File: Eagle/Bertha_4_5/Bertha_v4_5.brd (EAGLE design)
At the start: 100 x 83.6 mm, 132 parts, among them CON1 JACK_DC_BARREL, CON2 JACK_DC_BARREL, IC1 MCP1703DB, IC4 DRV8811, J1 RJ12RIGHTANGLE-I2C, J2 RJ12RIGHTANGLE-I2C, Q5 BSP75, Q6 BSP75, U1 HX711, U100 RN2483, X1 1503_09, X2 8MHz, X3 FH12-08S-1SH, X4 MINI-USB

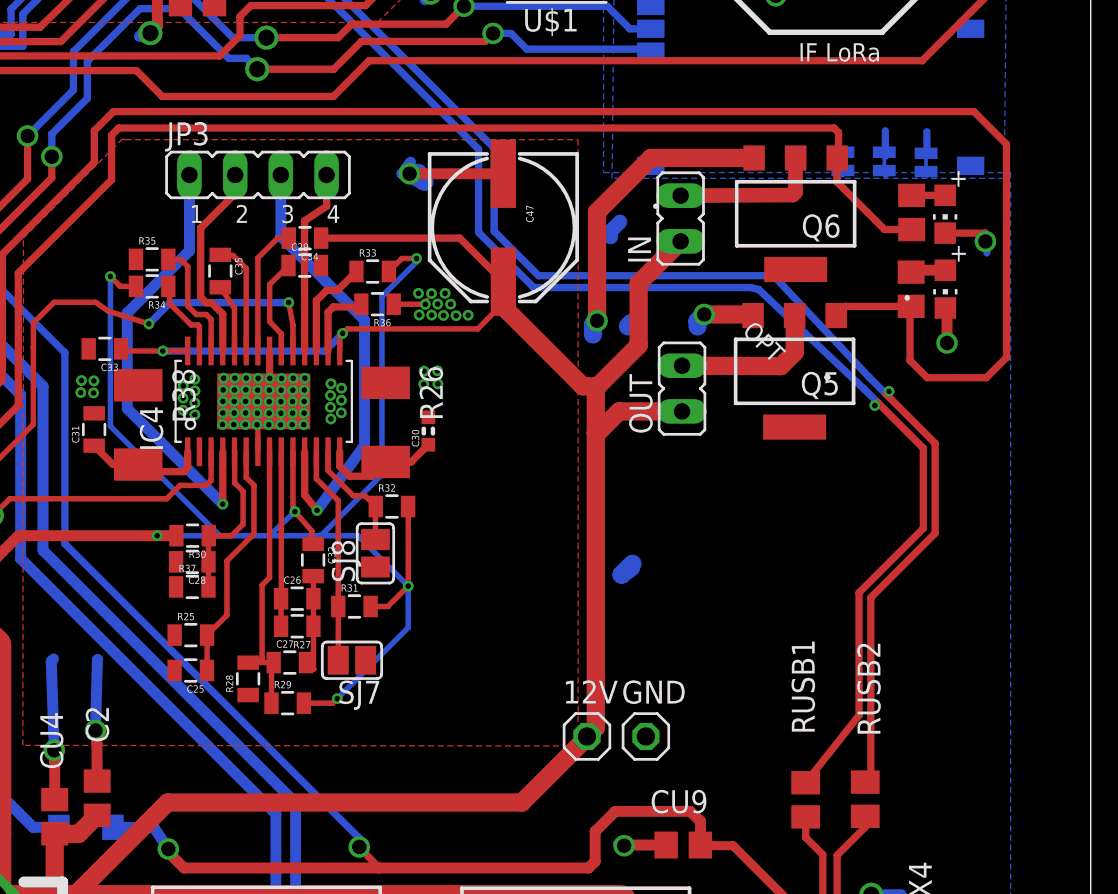
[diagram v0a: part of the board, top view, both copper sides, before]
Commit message: Moved pumps downward to prepare for LoRa antenna migration
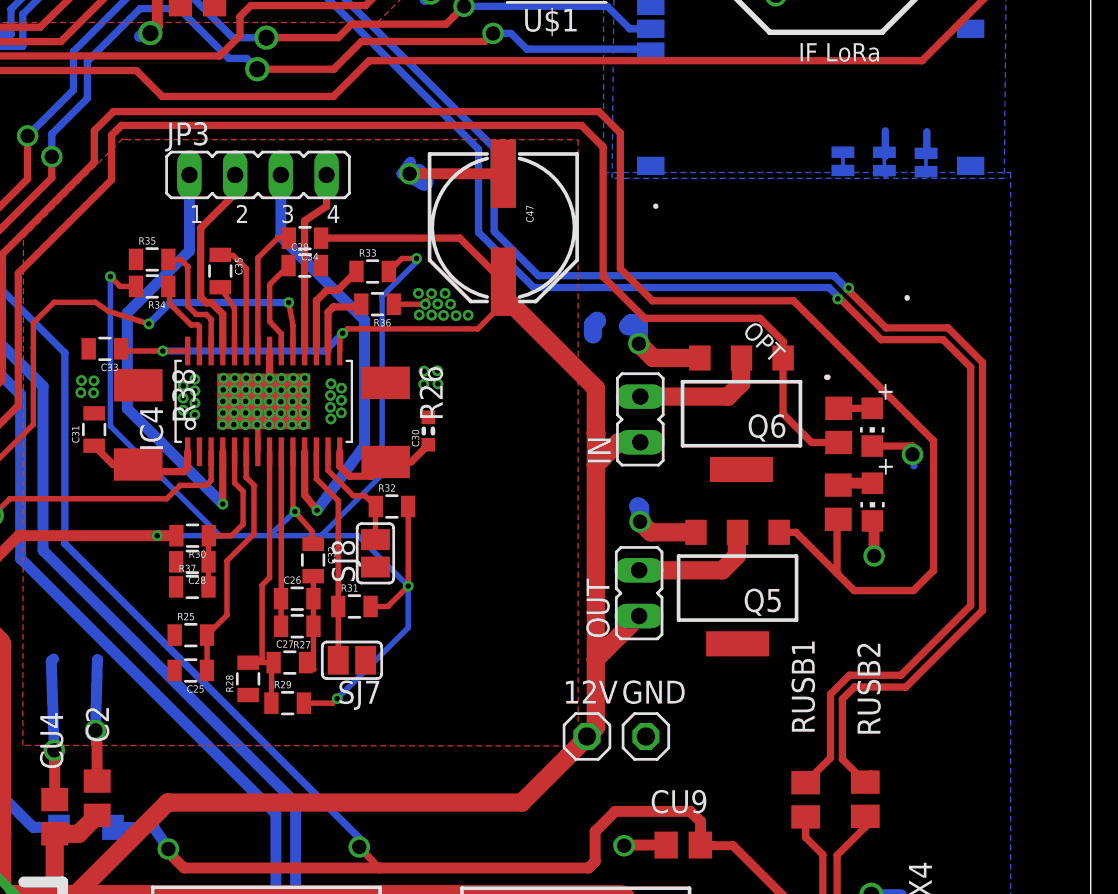
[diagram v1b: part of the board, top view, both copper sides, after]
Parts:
- moved RK12 12.5 mm to (81.0, 35.4)
- moved LDIN 12.5 mm to (82.9, 35.3)
- moved LDOUT 12.5 mm to (82.9, 31.1)
- moved RK13 12.5 mm to (81.0, 31.1)
- moved Q5 12.5 mm to (75.4, 26.3)
- moved OUT 11.6 mm to (69.9, 26.1)
- moved Q6 11.5 mm to (75.6, 36.0)
- moved IN 11.4 mm to (70.0, 35.7)
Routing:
- net GND: track 172.6 -> 159.4 mm
- net USB_P: track 111.2 -> 120.5 mm
- net +12V: track 244.9 -> 235.8 mm
- net USB_N: track 109.6 -> 117.7 mm
- net N$8: track 78.5 -> 84.3 mm
- net N$11: track 102.2 -> 104.5 mm
- net N$13: track 8.64 -> 7.09 mm
- net N$17: track 8.36 -> 7.33 mm
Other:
- board text added: "PUMPS"

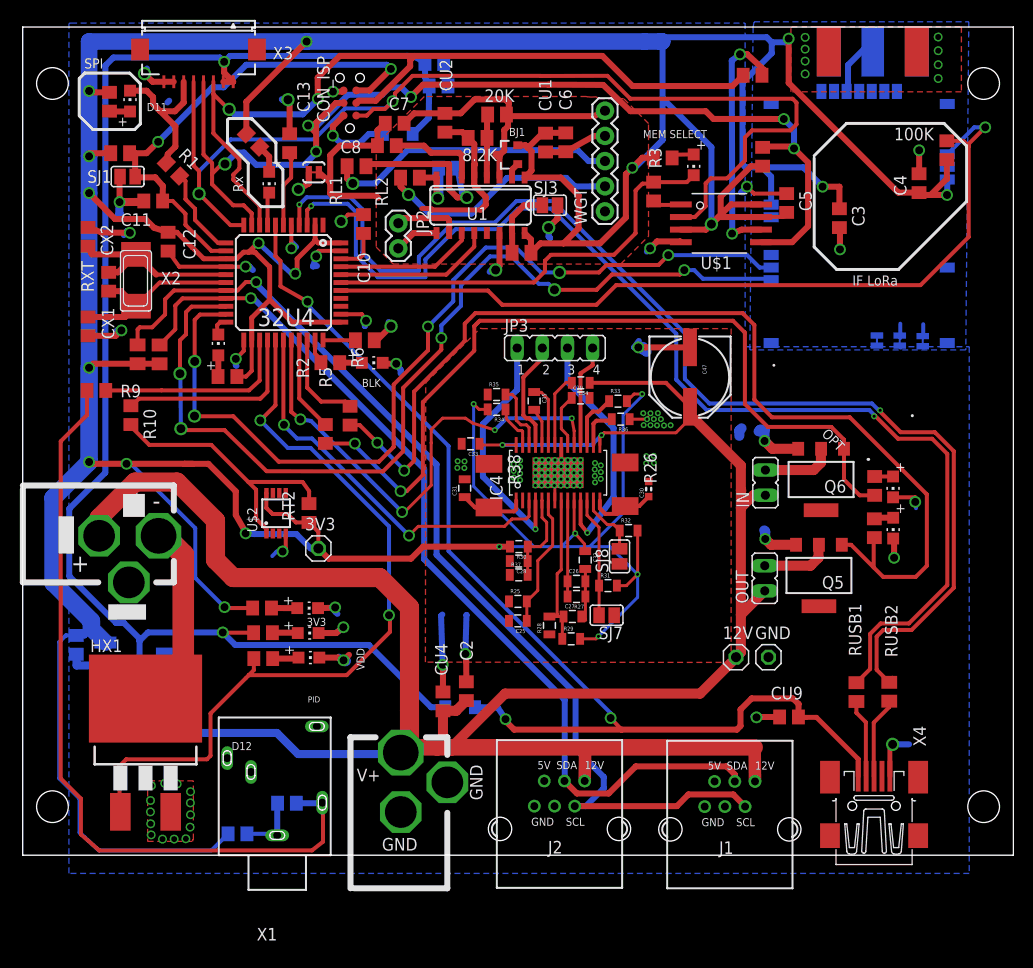
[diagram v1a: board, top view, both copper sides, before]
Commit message: LoRa Antenna moved inward, rerouted more simply the SST Flash memory closes #85 closes #86 closes #87, need to regen Gerbers
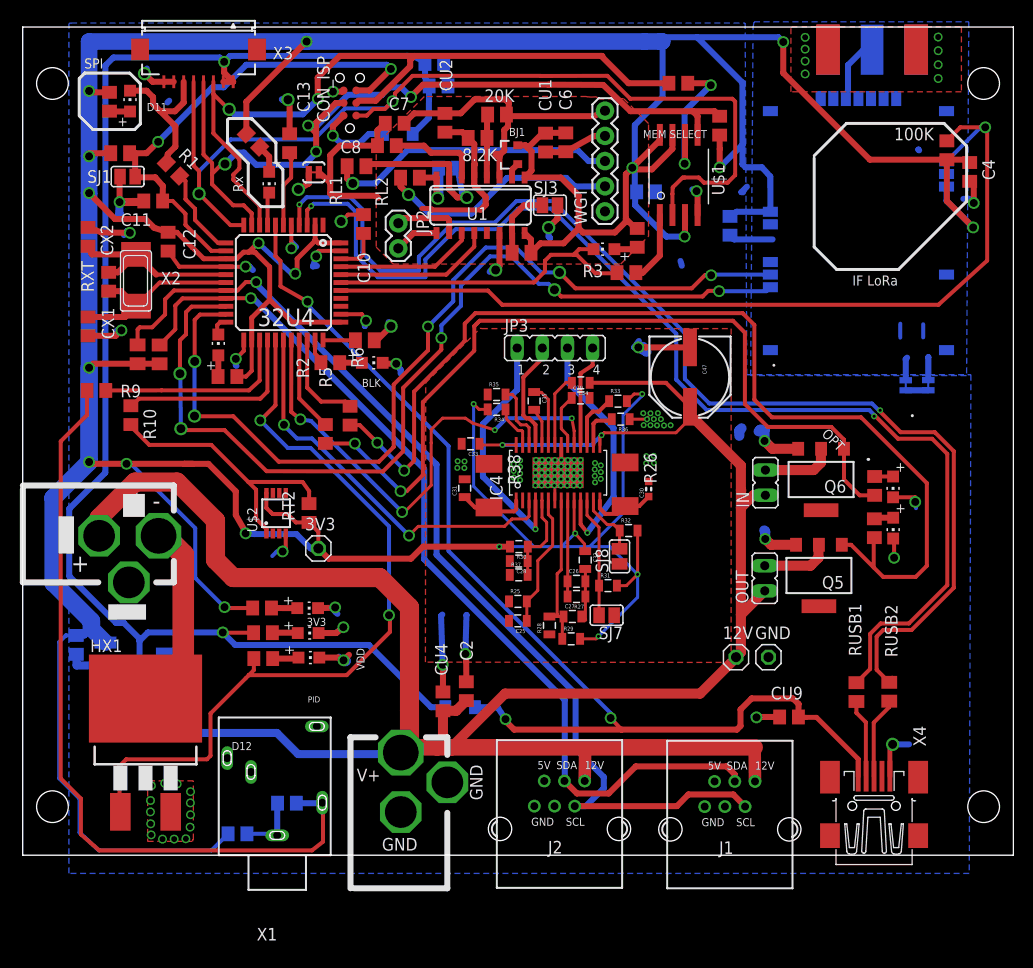
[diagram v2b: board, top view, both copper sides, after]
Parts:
- removed SJ6: (no value), SparkFun-Passives:PAD-JUMPER-2-NC_BY_TRACE_YES_SILK
- U$1: value SST25VF064C -> SST26VF064B
- moved C5 14.2 mm to (57.9, 65.1), flipped to the bottom, turned to 0 degrees
- moved LDMEM 12.4 mm to (53.7, 59.3), turned to 90 degrees
- moved C3 11.1 mm to (66.4, 61.6), flipped to the bottom
- moved R3 8.63 mm to (55.9, 56.9), turned to 180 degrees
- moved RK19 8.47 mm to (57.0, 60.4), turned to 270 degrees
- moved RK3 7.54 mm to (61.2, 76.0)
- moved SJ5 5.37 mm to (84.1, 45.5)
- moved RK4 5.36 mm to (65.4, 71.7)
- moved SJ4 5.34 mm to (86.4, 45.5)
- moved C4 5.24 mm to (90.6, 67.1), turned to 270 degrees
- moved U$1 4.91 mm to (61.2, 65.7), turned to 0 degrees
- moved U100 0.72 mm to (88.3, 47.8)
- moved 868MHZ 0.19 mm to (80.7, 82.0)
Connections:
- net ANGND: no longer SJ6.2
- net GND: no longer SJ6.1
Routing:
- net MOSI: track 109.8 -> 85.2 mm, vias 6 -> 4
- net N$23: track 25.2 -> 14.4 mm
- net A3: track 43.3 -> 32.7 mm
- net 3.3V: track 574.8 -> 565.1 mm
- net MISO: track 110.1 -> 100.9 mm
- net SCK: track 84.9 -> 76.9 mm
- net ANGND: track 7.76 -> 15.6 mm, vias 10 -> 9
- net A2: track 86.0 -> 90.9 mm
- net MEM_SEL: track 2.93 -> 7.23 mm
- net GND: track 159.4 -> 156.6 mm, vias 119 -> 118
- net N$11: track 104.5 -> 105.2 mm
- net RX: track 95.7 -> 95.1 mm
- net ANT868: track 5.91 -> 6.50 mm

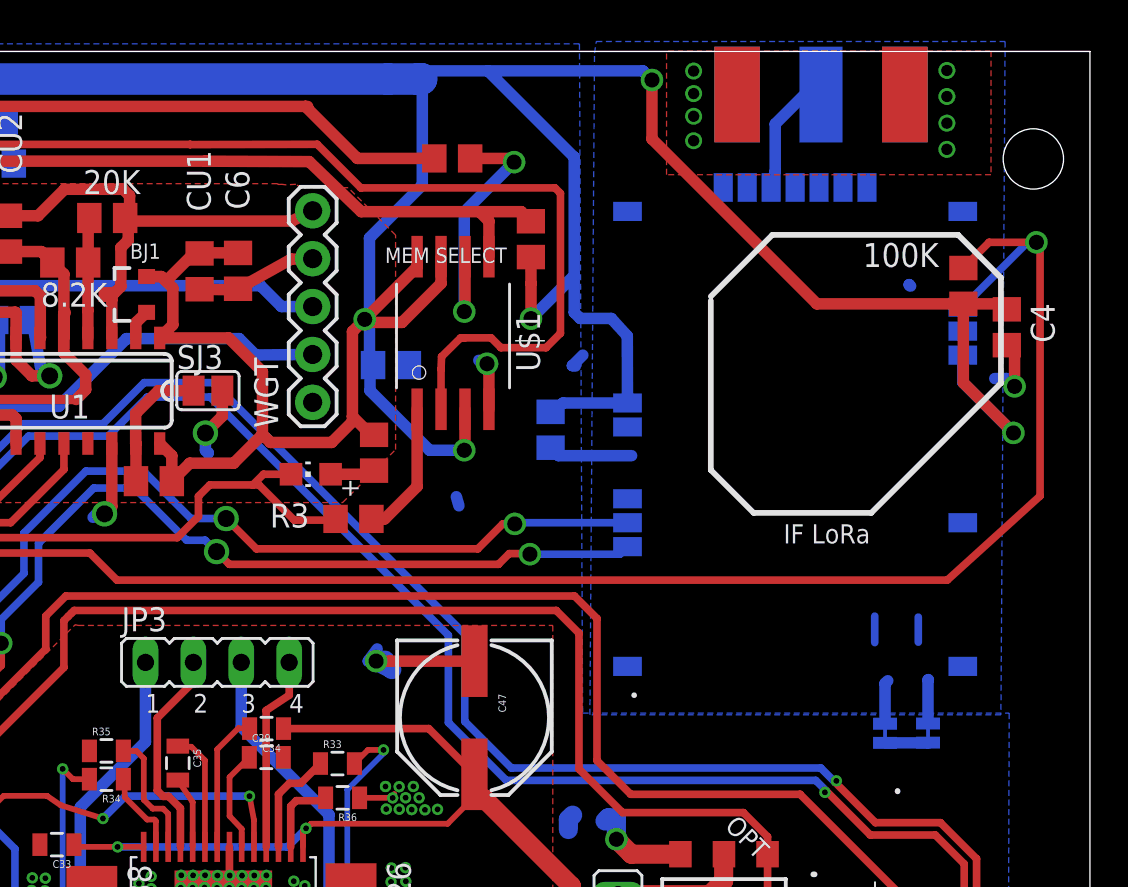
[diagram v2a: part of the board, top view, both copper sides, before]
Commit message: Modified LoRa footprint for ease of soldering Still need to regen Gerbers
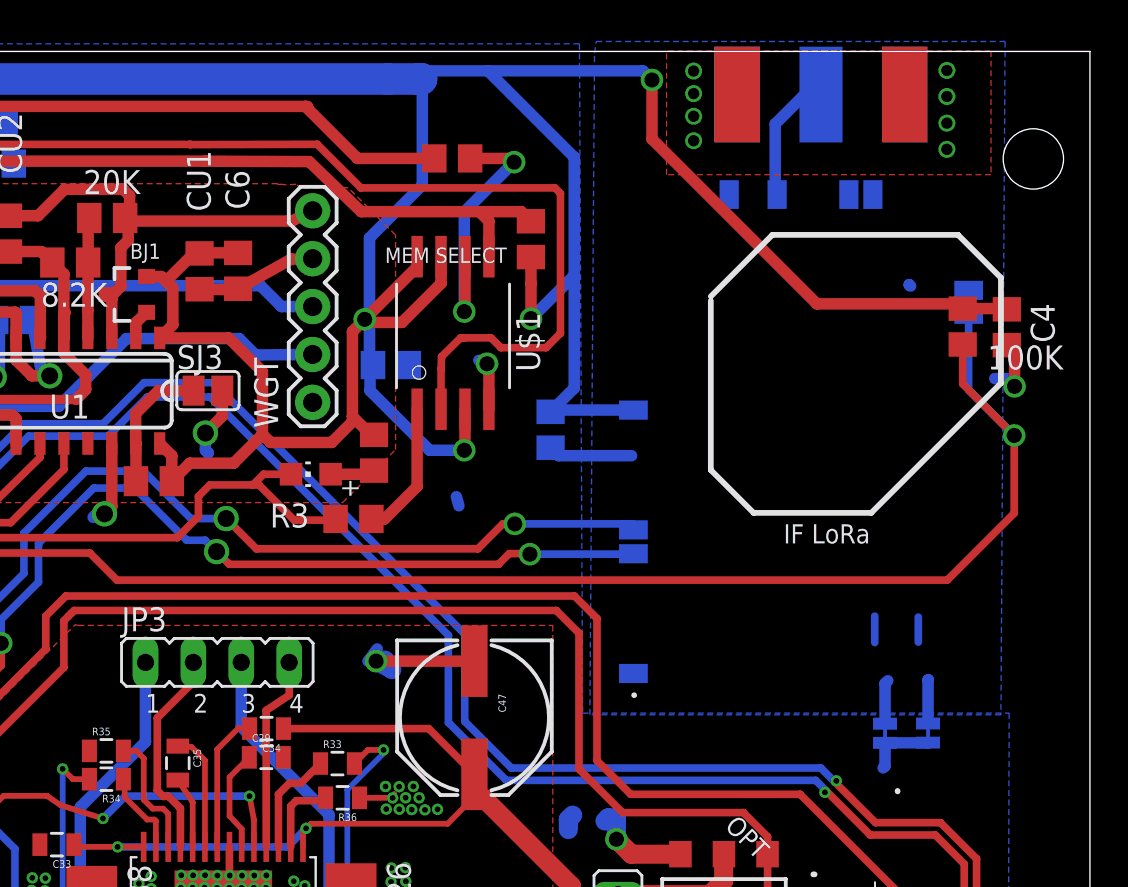
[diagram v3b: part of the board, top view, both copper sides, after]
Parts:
- removed U100: RN2483, Octanis1:RN2483
- added U$3: RN2483_SIMPLE, Octanis1_bioreactorPort:RN2483_SIMPLE
- moved 100K 2.16 mm to (88.3, 67.1), turned to 270 degrees
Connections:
- net 3.3V: now also U$3.P$12; no longer U100.P$12, U100.P$34
- net A2: now also U$3.P$32; no longer U100.P$32
- net ANGND: now also U$3.P$1, U$3.P$21, U$3.P$26, U$3.P$27, U$3.P$33; no longer U100.P$1, U100.P$11, U100.P$20, U100.P$21, U100.P$22, U100.P$24, U100.P$26, U100.P$27, U100.P$28, U100.P$33, U100.P$41, U100.P$47, U100.P$8
- net ANT868: now also U$3.P$23; no longer U100.P$23
- net RX: now also U$3.P$6; no longer U100.P$6
- net TX: now also U$3.P$7; no longer U100.P$7
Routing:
- net 3.3V: track 565.1 -> 551.4 mm, vias 22 -> 21
- net A2: track 90.9 -> 83.5 mm
- net TX: track 90.7 -> 91.4 mm

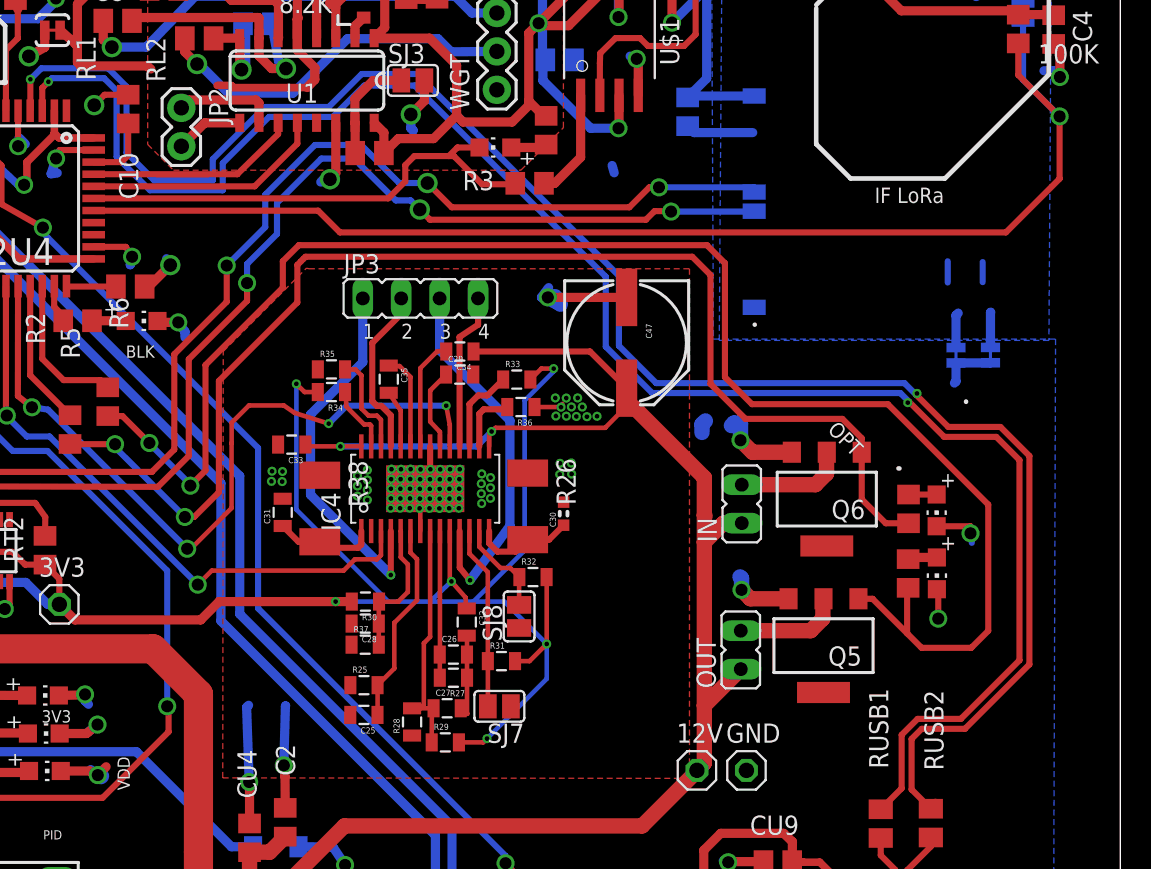
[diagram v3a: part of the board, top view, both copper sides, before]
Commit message: Added LEDs for DRV8811 Stepper Driver closes #83
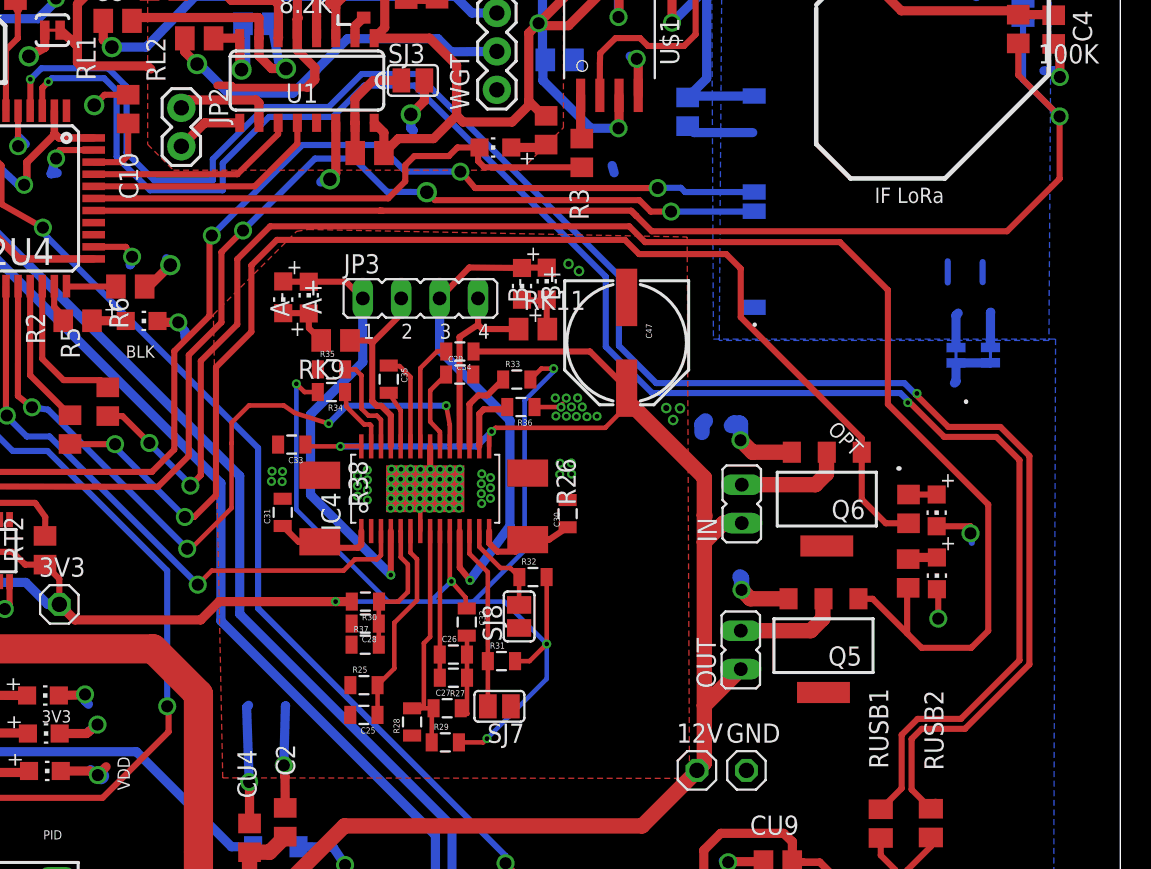
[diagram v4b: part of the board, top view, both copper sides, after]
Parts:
- added A+: A+, adafruit:CHIP-LED0805
- added A-: A-, adafruit:CHIP-LED0805
- added B+: B+, adafruit:CHIP-LED0805
- added B-: B-, adafruit:CHIP-LED0805
- added RK11, RK9: 10k, rcl:R0805
- C30: device freetronics-master-v1:0603 -> freetronics-master-v1:0805
- moved R3 3.99 mm to (59.4, 58.9), turned to 270 degrees
- moved C30 0.27 mm to (58.5, 35.1)
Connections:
- removed net N$10: IC4.25, JP3.2
- removed net N$4: IC4.18, JP3.4
- removed net N$55: IC4.4, JP3.1
- removed net N$56: IC4.11, JP3.3
- new net AOUT1: A+.A, A-.C, IC4.4, JP3.1
- new net AOUT2: IC4.25, JP3.2, RK9.1
- new net BOUT1: B+.A, B-.C, IC4.11, JP3.3
- new net BOUT2: IC4.18, JP3.4, RK11.1
- new net N$15: A+.C, A-.A, RK9.2
- new net N$19: B+.C, B-.A, RK11.2
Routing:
- net BOUT1: track 0.00 -> 33.0 mm, vias 0 -> 1
- net AOUT1: track 0.00 -> 30.8 mm, vias 0 -> 1
- net N$56: track 24.9 -> 0.00 mm, vias 1 -> 0
- net N$55: track 24.8 -> 0.00 mm, vias 1 -> 0
- net BOUT2: track 0.00 -> 13.3 mm
- net AOUT2: track 0.00 -> 12.8 mm
- net N$10: track 11.3 -> 0.00 mm
- net N$4: track 10.5 -> 0.00 mm
- net GND: track 157.0 -> 149.1 mm, vias 118 -> 122
- net MEM_SEL: track 7.23 -> 2.89 mm
- net N$19: track 0.00 -> 4.31 mm
- net N$15: track 0.00 -> 4.11 mm
- net N$11: track 105.2 -> 108.1 mm
- net A3: track 32.7 -> 35.5 mm
- net TX: track 91.4 -> 90.8 mm
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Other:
- board text added: "PhA1"
- board text added: "PhA2"
- board text added: "PhB1"
- board text added: "PhB2"
